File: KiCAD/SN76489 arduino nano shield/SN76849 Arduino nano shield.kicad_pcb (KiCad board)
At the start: 2 copper layers, 4.4 x 24.3 mm, 1 part, among them U1 PCF8574

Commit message: Printplaat 20180601 0.5 laat maak
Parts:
- added C2_10uF: CP_10uF, Capacitors_THT:CP_Radial_D8.0mm_P2.50mm, F.Cu at (68.0, 25.0)
- added C3_220uF: CP_220uF, Capacitors_THT:CP_Radial_D8.0mm_P2.50mm, F.Cu at (79.5, 51.5)
- added G***: LOGO, lib_michiel:Sovjet_simpits_logo01, F.Cu at (48.5, 37.8)
- added J1: Arduino_sn, Socket_Strips:Socket_Strip_Angled_1x03_Pitch2.54mm, F.Cu at (36.1, 28.4)
- added J2: audio_debug, Socket_Strips:Socket_Strip_Straight_1x02_Pitch2.54mm, F.Cu at (79.0, 24.0)
- added P1: Audio_uit, Socket_Strips:Socket_Strip_Angled_1x03_Pitch2.54mm, F.Cu at (48.3, 29.0)
- added P3: I2C, Socket_Strips:Socket_Strip_Angled_1x03_Pitch2.54mm, F.Cu at (65.0, 49.0)
- added R2: R1k, w_pth_resistors:RC03, F.Cu at (57.4, 24.4)
- added REF***: OSHW-Logo, Symbols:OSHW-Logo2_7.3x6mm_SilkScreen, F.Cu at (92.0, 46.0)
- added RV1: POT_50k, w_pth_resistors:trimmer_ecp_ca9-v10, F.Cu at (87.5, 37.5)
- added U2: LM358, w_pth_circuits:dil_8-300_socket, F.Cu at (69.0, 39.0)
- added U3: SN76489, w_pth_circuits:dil_16-300_socket, F.Cu at (33.0, 46.0)
- U1: value PCF8574 -> PCF8574P
- moved U1 24.1 mm to (51.0, 46.0), turned to 270 degrees
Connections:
- net /CE renamed GND
- U1 pad 10: /D2 -> /P5
- U1 pad 11: /D1 -> /P6
- U1 pad 12: /D0 -> /P7
- U1 pad 4: /D7 -> /P0
- U1 pad 5: /D6 -> /P1
- U1 pad 6: /D5 -> /P2
- U1 pad 7: /D4 -> /P3
- U1 pad 9: /D3 -> /P4
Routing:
- net (no net): track 416.6 -> 0.00 mm
- net GND: track 7.81 -> 123.4 mm, vias 0 -> 3
- net /P4: track 0.00 -> 77.1 mm, vias 0 -> 3
- net /Audio: track 0.00 -> 68.9 mm
- net /P5: track 0.00 -> 56.7 mm, vias 0 -> 3
- net Net-(P1-Pad1): track 0.00 -> 52.4 mm
- net /P6: track 0.00 -> 46.8 mm, vias 0 -> 2
- net /P7: track 0.00 -> 45.4 mm, vias 0 -> 3
- net /VCC: track 22.0 -> 65.6 mm
- net /P3: track 0.00 -> 33.2 mm, vias 0 -> 3
- net Net-(C3-Pad1): track 0.00 -> 30.3 mm, vias 0 -> 1
- net Net-(C2-Pad2): track 0.00 -> 24.6 mm
- net /WE: track 0.00 -> 22.1 mm, vias 0 -> 1
- net /D3: track 19.6 -> 0.00 mm
- net /D5: track 18.2 -> 0.00 mm
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- removed copper zone on B.Cu, net (none)
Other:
- board size 4.4 x 24.3 mm -> 74.2 x 45.8 mm
- board text added: "Arduino"
- board text added: "BBC Micro retroSynth versie: 20180601 0.4"
- board text added: "CLK"
- board text added: "Elkeen het ingebore waardigheid en die reg dat daardie waardigheid gerespekteer en beskerm word."
- board text added: "GND"
- board text added: "Geluid_uit"
- board text added: "Links"
- board text added: "Ontwerp: Michiel Erasmus thebapodcast@gmail.com #s4kdh"
- board text added: "R1k"
- board text added: "Regs"
- board text added: "VCC"
- board text added: "Volume beheer"
- board text added: "WE"
- board text added: "geluid_debug"

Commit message: Printplaat 20180601 0.6 i2C silkS SDA toegevoegd
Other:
- board text added: "Arduino-I2C"
- board text added: "BBC Micro retroSynth versie: 20180602 0.6"
- board text added: "Ontwerp: Michiel Erasmus thebapodcast@gmail.com"
- board text added: "SDA"
- board text removed: "BBC Micro retroSynth versie: 20180601 0.4"
- board text removed: "Ontwerp: Michiel Erasmus thebapodcast@gmail.com #s4kdh"
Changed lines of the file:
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@@
     (area 23.424999 16.424999 98.075001 62.325001)
     (thickness 1.6)
-    (drawings 41)
+    (drawings 45)
     (tracks 354)
     (zones 0)
@@
     (title "EasyLab chiptunes")
     (date 2018-06-02)
-    (rev "20180601 0.5")
+    (rev "20180602 0.6")
     (company "©2018 EasyLab4Kids en Michiel Erasmus")
     (comment 3 "versie 20180330")
@@
       (xy 3.64768 5.945169)) (layer F.SilkS) (width 0.01))
   )
+  (gr_text "Ontwerp: Michiel Erasmus thebapodcast@gmail.com" (at 46.5 59.5) (layer F.SilkS)
+    (effects (font (size 0.8 0.8) (thickness 0.2)))
+  )
+  (gr_text Arduino-I2C (at 67.5 59.75) (layer F.SilkS)
+    (effects (font (size 0.7 0.7) (thickness 0.175)))
+  )
+  (gr_text VCC (at 70 47) (layer F.SilkS)
+    (effects (font (size 0.7 0.7) (thickness 0.175)))
+  )
+  (gr_text SDA (at 67.5 47) (layer F.SilkS)
+    (effects (font (size 0.7 0.7) (thickness 0.175)))
+  )
+  (gr_text SDA (at 64.75 47) (layer F.SilkS)
+    (effects (font (size 0.7 0.7) (thickness 0.175)))
+  )
   (gr_text "Elkeen het ingebore waardigheid en die reg dat\ndaardie waardigheid gerespekteer en beskerm word." (at 43 20) (layer B.SilkS)
     (effects (font (size 0.7 0.7) (thickness 0.175)) (justify mirror))
@@
   (gr_line (start 29 59.5) (end 26 59.5) (angle 90) (layer Edge.Cuts) (width 0.15))
   (gr_line (start 30.5 61) (end 29 59.5) (angle 90) (layer Edge.Cuts) (width 0.15))
-  (gr_text "Ontwerp: Michiel Erasmus thebapodcast@gmail.com    #s4kdh" (at 51 59.75) (layer F.SilkS)
-    (effects (font (size 0.8 0.8) (thickness 0.2)))
-  )
   (gr_text R1k (at 55.75 24.25 90) (layer F.SilkS)
     (effects (font (size 0.7 0.7) (thickness 0.175)))
@@
     (effects (font (size 0.8 0.8) (thickness 0.2)))
   )
-  (gr_text "BBC Micro retroSynth versie: 20180601 0.4" (at 44 58) (layer F.SilkS)
+  (gr_text "BBC Micro retroSynth versie: 20180602 0.6" (at 44 58) (layer F.SilkS)
     (effects (font (size 0.8 0.8) (thickness 0.2)))
   )

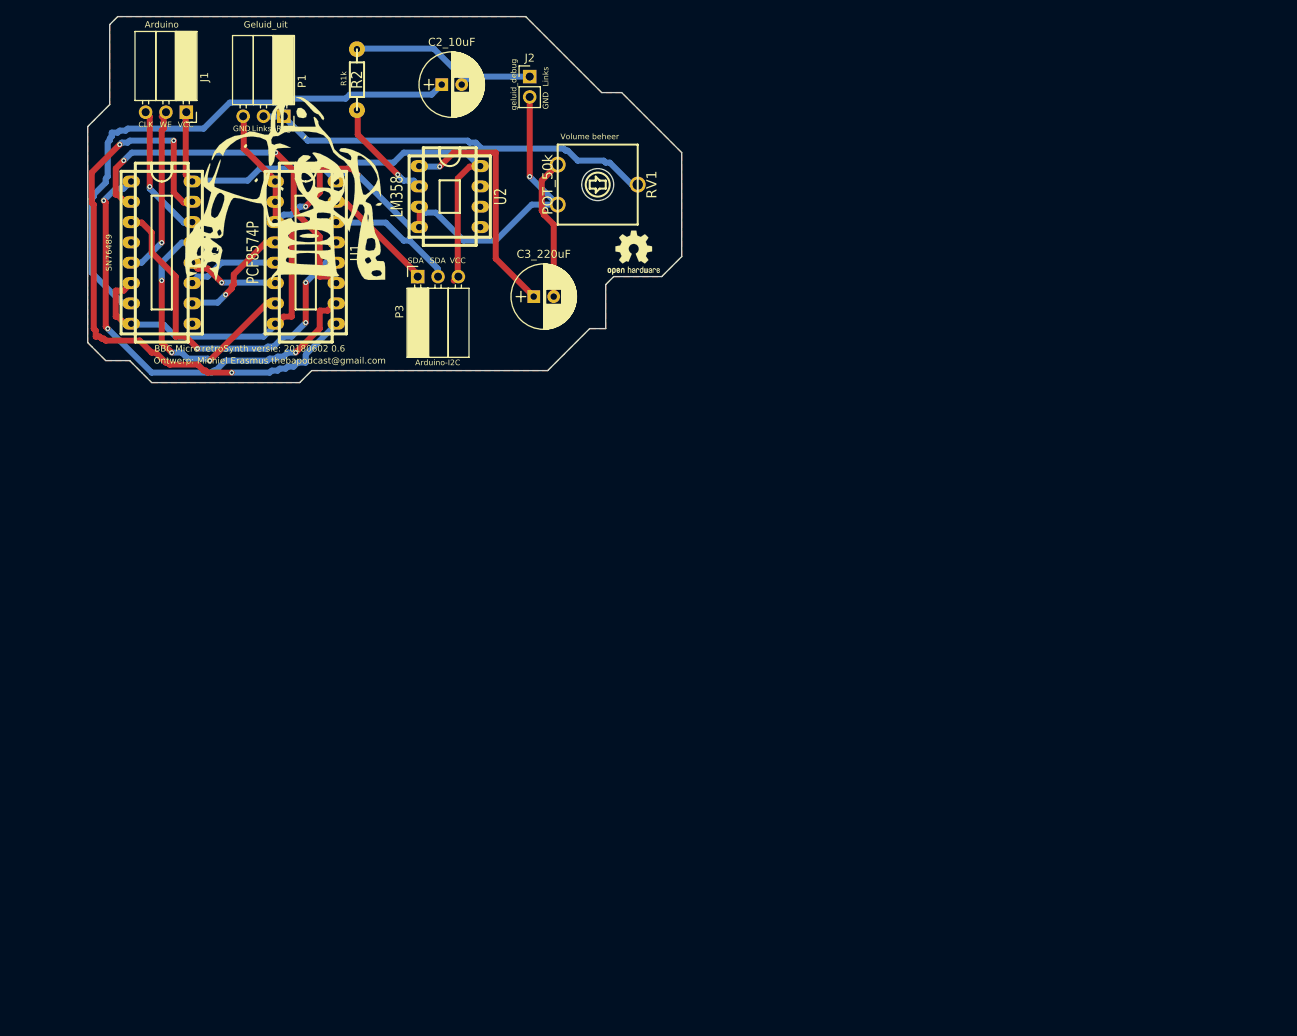
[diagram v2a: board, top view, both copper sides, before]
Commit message: toevoeging OpAmp schema en PCB 20180617 0.7
daar is nog een bug. Op printplaat capacitor C1 posetief niet
verobonden!
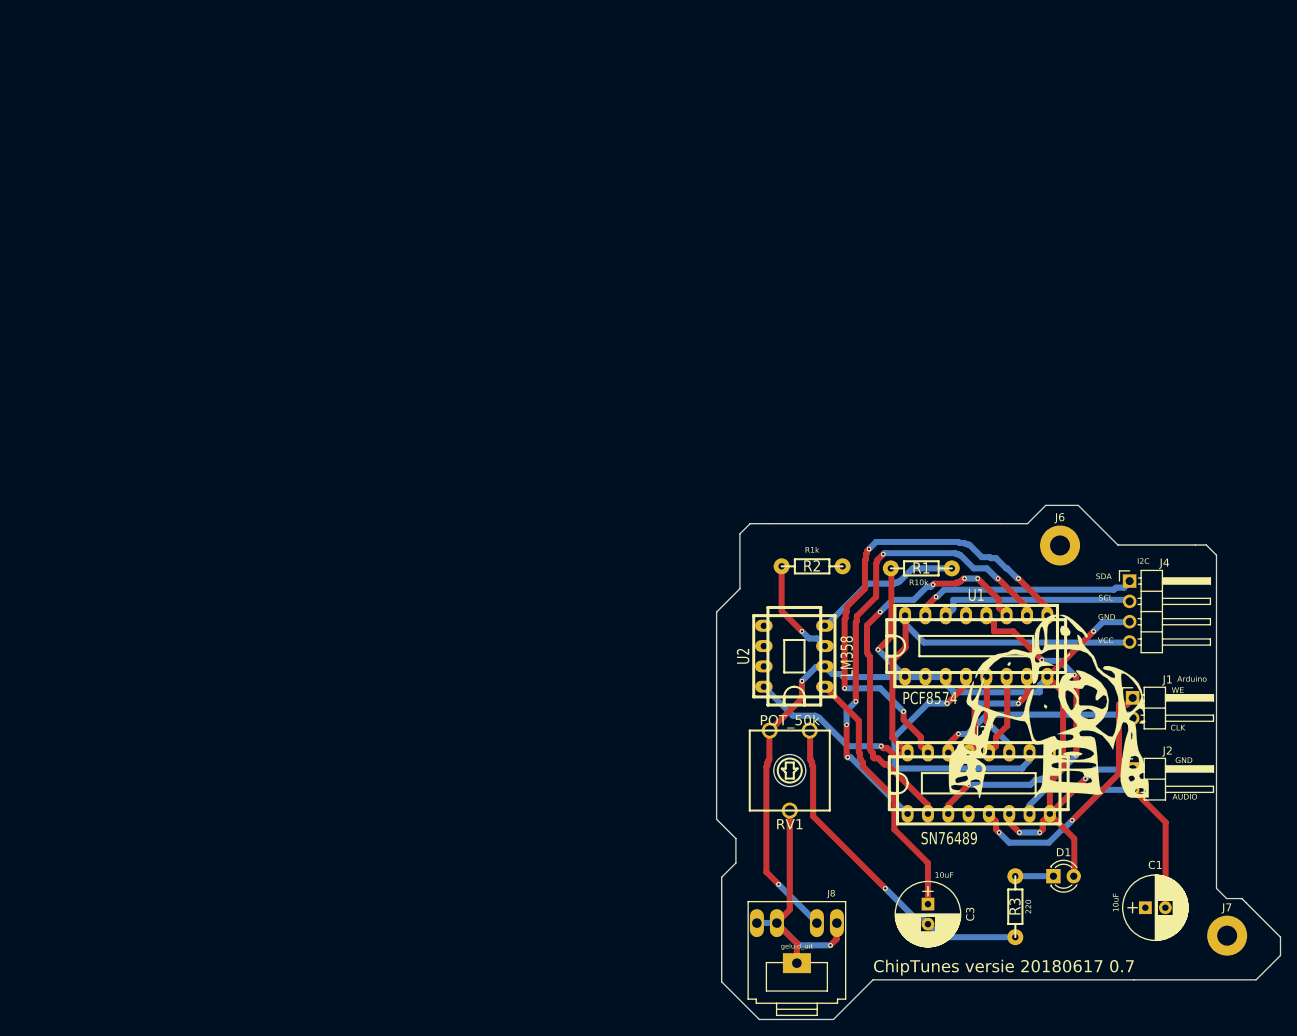
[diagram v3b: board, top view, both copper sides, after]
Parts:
- removed C2_10uF: CP_10uF, Capacitors_THT:CP_Radial_D8.0mm_P2.50mm
- removed C3_220uF: CP_220uF, Capacitors_THT:CP_Radial_D8.0mm_P2.50mm
- removed G***: LOGO, lib_michiel:Sovjet_simpits_logo01
- removed P1: Audio_uit, Socket_Strips:Socket_Strip_Angled_1x03_Pitch2.54mm
- removed P3: I2C, Socket_Strips:Socket_Strip_Angled_1x03_Pitch2.54mm
- removed REF***: OSHW-Logo, Symbols:OSHW-Logo2_7.3x6mm_SilkScreen
- added C1: CP_220uF, Capacitors_THT:CP_Radial_D8.0mm_P2.50mm, F.Cu at (156.0, 127.9)
- added C3: CP_220uF, Capacitors_THT:CP_Radial_D8.0mm_P2.50mm, F.Cu at (128.8, 127.4)
- added D1: Liggie, LEDs:LED_D3.0mm, F.Cu at (144.5, 124.0)
- added J4: I2C, Pin_Headers:Pin_Header_Angled_1x04_Pitch2.54mm, F.Cu at (154.0, 87.1)
- added J5: LOGO, lib_michiel:Sovjet_simpits_logo01, F.Cu at (144.0, 102.5)
- added J6: gat1, Mounting_Holes:MountingHole_2.5mm_Pad, F.Cu at (145.3, 82.6)
- added J7: gat2, Mounting_Holes:MountingHole_2.5mm_Pad, F.Cu at (166.2, 131.4)
- added J8: geluid_uit, lib_michiel:3.5mm_stereo_TRS_jack_A-853_Tayda_, F.Cu at (112.4, 133.2)
- added R1: R10k, w_pth_resistors:RC03, F.Cu at (128.0, 85.5)
- added R3: 220, w_pth_resistors:RC03, F.Cu at (139.7, 127.8)
- J1: footprint Socket_Strips:Socket_Strip_Angled_1x03_Pitch2.54mm -> Pin_Headers:Pin_Header_Angled_1x02_Pitch2.54mm
- J2: footprint Socket_Strips:Socket_Strip_Straight_1x02_Pitch2.54mm -> Pin_Headers:Pin_Header_Angled_1x02_Pitch2.54mm
- U1: value PCF8574P -> PCF8574
- moved J1 139.1 mm to (154.4, 101.7), turned to 0 degrees
- moved U3 121.8 mm to (135.1, 112.3), turned to 0 degrees
- moved J2 114.8 mm to (154.4, 110.6)
- moved U1 97.2 mm to (134.8, 95.2), turned to 0 degrees
- moved R2 83.3 mm to (114.3, 85.2), turned to 0 degrees
- moved RV1 77.1 mm to (111.5, 110.7), turned to 0 degrees
- moved U2 71.8 mm to (112.1, 96.5), turned to 90 degrees
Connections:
- J1 pad 1: /VCC -> /WE
- J1 pad 2: /WE -> /Clock
- J2 pad 1: Net-(C2-Pad2) -> GND
- J2 pad 2: GND -> /Audio
- R2 pad 2: Net-(C2-Pad2) -> /Audio
- U2 pad 2: Net-(R2-Pad1) -> GND
- U2 pad 3: GND -> Net-(R2-Pad1)
- U2 pad 4: GND -> Net-(R1-Pad2)
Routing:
- net /Audio: track 68.9 -> 31.2 mm
- net GND: track 123.4 -> 148.2 mm, vias 3 -> 7
- net Net-(C2-Pad2): track 24.6 -> 0.00 mm
- net Net-(C3-Pad2): track 18.0 -> 42.5 mm, vias 0 -> 1
- net /P0: track 14.7 -> 35.0 mm
- net Net-(R1-Pad2): track 0.00 -> 18.8 mm
- net Net-(J8-Pad1): track 52.4 -> 34.5 mm, vias 0 -> 1
- net /P3: track 33.2 -> 15.6 mm, vias 3 -> 2
- net /P4: track 77.1 -> 61.0 mm, vias 3 -> 4
- net /SDA: track 14.8 -> 28.1 mm, vias 0 -> 1
- net /WE: track 22.1 -> 32.8 mm, vias 1 -> 2
- net /Clock: track 16.9 -> 25.8 mm
- net /SCL: track 16.3 -> 24.6 mm
- net /VCC: track 65.6 -> 70.6 mm, vias 0 -> 1
- net Net-(D1-Pad1): track 0.00 -> 4.76 mm
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- removed copper zone on F.Cu, net (none)
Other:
- board size 74.2 x 45.8 mm -> 70.5 x 64.3 mm
- board text added: "10uF"
- board text added: "220"
- board text added: "AUDIO"
- board text added: "ChipTunes versie 20180617 0.7"
- board text added: "I2C"
- board text added: "R10k"
- board text added: "SCL"
- board text removed: "Arduino-I2C"
- board text removed: "BBC Micro retroSynth versie: 20180602 0.6"
- board text removed: "Elkeen het ingebore waardigheid en die reg dat daardie waardigheid gerespekteer en beskerm word."
- board text removed: "Geluid_uit"
- board text removed: "Links"
- board text removed: "Ontwerp: Michiel Erasmus thebapodcast@gmail.com"
- board text removed: "Regs"
- board text removed: "Volume beheer"
- board text removed: "geluid_debug"

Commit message: DERC fails opgelost 20180617 0.7.01
'n paar nets ontbreekte conneksies op de printplaat.
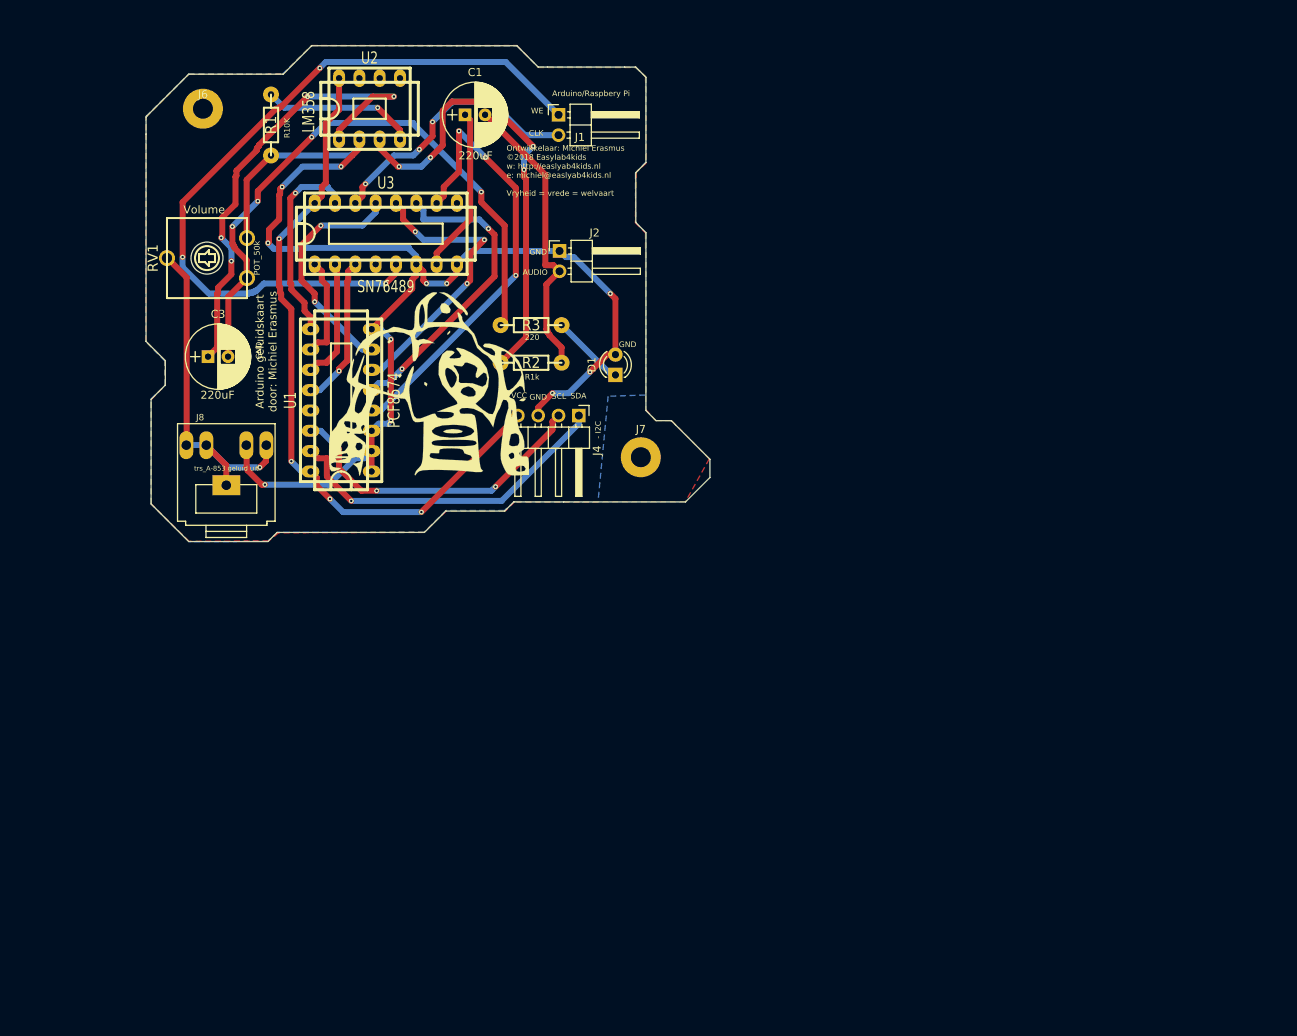
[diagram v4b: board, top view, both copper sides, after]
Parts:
- J8: value geluid_uit -> trs_A-853 geluid uit
- moved C1 130.6 mm to (70.9, 28.8)
- moved J6 120.2 mm to (38.2, 28.0)
- moved C3 113.1 mm to (38.8, 59.0), turned to 0 degrees
- moved J1 102.3 mm to (82.6, 28.8)
- moved U3 101.1 mm to (61.0, 43.6)
- moved R1 98.4 mm to (46.7, 30.0), turned to 90 degrees
- moved RV1 97.0 mm to (38.7, 46.7), turned to 270 degrees
- moved J2 96.6 mm to (82.7, 45.8)
- moved J7 94.6 mm to (92.9, 71.6)
- moved R3 94.6 mm to (79.2, 55.1), turned to 180 degrees
- moved J8 93.0 mm to (41.1, 73.5)
- moved J5 87.3 mm to (66.5, 62.2)
- moved U2 86.6 mm to (59.0, 28.0), turned to 0 degrees
- moved U1 85.1 mm to (55.4, 64.5), turned to 90 degrees
- moved D1 83.2 mm to (89.7, 61.3), turned to 90 degrees
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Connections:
- C1 pad 1: (no net) -> /Audio
- C1 pad 2: /Audio -> Net-(C1-Pad2)
- J2 pad 2: /Audio -> Net-(C1-Pad2)
- R2 pad 2: /Audio -> Net-(C1-Pad2)
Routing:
- net /WE: track 32.8 -> 95.3 mm, vias 2 -> 3
- net /P5: track 59.9 -> 12.8 mm, vias 5 -> 0
- net Net-(R2-Pad1): track 12.8 -> 58.6 mm, vias 1 -> 4
- net Net-(C1-Pad2): track 0.00 -> 36.9 mm
- net /P4: track 61.0 -> 25.1 mm, vias 4 -> 1
- net Net-(C3-Pad2): track 42.5 -> 77.0 mm, vias 1 -> 4
- net /P6: track 49.6 -> 15.4 mm, vias 4 -> 0
- net /P1: track 10.7 -> 38.5 mm, vias 1 -> 2
- net Net-(C3-Pad1): track 32.5 -> 59.3 mm, vias 0 -> 4
- net /P2: track 10.6 -> 36.4 mm, vias 0 -> 3
- net /P7: track 44.5 -> 18.7 mm, vias 4 -> 1
- net GND: track 148.2 -> 169.7 mm, vias 7 -> 11
- net /P0: track 35.0 -> 56.2 mm, vias 1 -> 3
- net /VCC: track 70.6 -> 88.2 mm, vias 1 -> 4
- net /SCL: track 24.6 -> 40.0 mm, vias 0 -> 3
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- added copper zone on B.Cu, net (none)
- added copper zone on F.Cu, net (none)
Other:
- board size 70.5 x 64.3 mm -> 70.5 x 62 mm
- board text added: "- I2C"
- board text added: "220uF"
- board text added: "Arduino geluidskaart door: Michiel Erasmus"
- board text added: "Arduino/Raspbery Pi"
- board text added: "Ontwikkelaar: Michiel Erasmus ©2018 Easylab4kids w: http://easlyab4kids.nl e: michiel@easlyab4kids.nl Vryheid = vrede = welvaart"
- board text added: "R10K"
- board text added: "Volume"
- board text removed: "10uF"
- board text removed: "Arduino"
- board text removed: "ChipTunes versie 20180617 0.7"
- board text removed: "I2C"
- board text removed: "R10k"
